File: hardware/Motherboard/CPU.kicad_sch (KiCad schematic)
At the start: 16 parts, among them U1 MC6809, U10 74LS138, U2 27C64, U3 74LS245, U4 74LS139, U5 74LS20, U6 74LS08, U7 74LS02, U8 74LS00, U9 74LS541

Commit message: wip
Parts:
- removed unit 4 of U7
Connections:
- net SYS_ROM_BK: now reaches U2.2 (A12)
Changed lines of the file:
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@@
 	)
 	(junction
-		(at 226.06 162.56)
+		(at 322.58 82.55)
 		(diameter 0)
 		(color 0 0 0 0)
 	)
 	(junction
-		(at 322.58 82.55)
+		(at 215.9 151.13)
 		(diameter 0)
 		(color 0 0 0 0)
@@
 		(color 0 0 0 0)
 	)
-	(junction
-		(at 210.82 151.13)
-		(diameter 0)
-		(color 0 0 0 0)
-	)
 	(no_connect
 		(at 177.8 247.65)
@@
 	(wire
 		(pts
-			(xy 210.82 162.56) (xy 226.06 162.56)
-		)
-		(stroke
-			(width 0)
-			(type default)
-		)
-	)
-	(wire
-		(pts
 			(xy 177.8 232.41) (xy 189.23 232.41)
 		)
@@
 		)
 	)
+	(wire
+		(pts
+			(xy 176.53 30.48) (xy 176.53 91.44)
+		)
+		(stroke
+			(width 0)
+			(type default)
+		)
+	)
 	(polyline
 		(pts
@@
 	(wire
 		(pts
-			(xy 210.82 151.13) (xy 228.6 151.13)
-		)
-		(stroke
-			(width 0)
-			(type default)
-		)
-	)
-	(wire
-		(pts
 			(xy 245.11 130.81) (xy 246.38 130.81)
 		)
@@
 		)
 	)
+	(wire
+		(pts
+			(xy 215.9 151.13) (xy 228.6 151.13)
+		)
+		(stroke
+			(width 0)
+			(type default)
+		)
+	)
 	(polyline
 		(pts
@@
 		)
 	)
+	(wire
+		(pts
+			(xy 176.53 91.44) (xy 186.69 91.44)
+		)
+		(stroke
+			(width 0)
+			(type default)
+		)
+	)
 	(polyline
 		(pts
@@
 	(wire
 		(pts
-			(xy 210.82 151.13) (xy 210.82 162.56)
+			(xy 215.9 151.13) (xy 215.9 162.56)
 		)
 		(stroke
@@
 	(wire
 		(pts
-			(xy 210.82 151.13) (xy 209.55 151.13)
+			(xy 209.55 151.13) (xy 215.9 151.13)
 		)
 		(stroke
@@
 	(wire
 		(pts
+			(xy 215.9 162.56) (xy 269.24 162.56)
+		)
+		(stroke
+			(width 0)
+			(type default)
+		)
+	)
+	(wire
+		(pts
 			(xy 185.42 115.57) (xy 246.38 115.57)
 		)
@@
 		)
 	)
-	(wire
-		(pts
-			(xy 226.06 160.02) (xy 228.6 160.02)
-		)
-		(stroke
-			(width 0)
-			(type default)
-		)
-	)
 	(polyline
 		(pts
@@
 		)
 	)
-	(wire
-		(pts
-			(xy 243.84 162.56) (xy 269.24 162.56)
-		)
-		(stroke
-			(width 0)
-			(type default)
-		)
-	)
 	(bus
 		(pts
@@
 		)
 	)
-	(wire
-		(pts
-			(xy 226.06 162.56) (xy 226.06 160.02)
-		)
-		(stroke
-			(width 0)
-			(type default)
-		)
-	)
 	(bus
 		(pts
@@
 	(wire
 		(pts
-			(xy 228.6 165.1) (xy 226.06 165.1)
-		)
-		(stroke
-			(width 0)
-			(type default)
-		)
-	)
-	(wire
-		(pts
 			(xy 69.85 78.74) (xy 69.85 85.09)
 		)
@@
 		)
 	)
+	(wire
+		(pts
+			(xy 30.48 30.48) (xy 176.53 30.48)
+		)
+		(stroke
+			(width 0)
+			(type default)
+		)
+	)
 	(bus
 		(pts
@@
 	(wire
 		(pts
-			(xy 226.06 165.1) (xy 226.06 162.56)
-		)
-		(stroke
-			(width 0)
-			(type default)
-		)
-	)
-	(wire
-		(pts
 			(xy 325.12 102.87) (xy 335.28 102.87)
 		)
@@
 		)
 	)
-	(label "VMA"
-		(at 264.16 162.56 0)
-		(effects
-			(font
-				(size 1.27 1.27)
-			)
-			(justify left bottom)
-		)
-	)
 	(label "A[15..0]"
 		(at 153.67 44.45 0)
@@
 		)
 	)
-	(hierarchical_label "VMA"
+	(hierarchical_label "~{VMA}"
 		(shape output)
 		(at 269.24 162.56 0)
@@
 		)
 	)
+	(hierarchical_label "SYS_ROM_BK"
+		(shape input)
+		(at 30.48 30.48 180)
+		(effects
+			(font
+				(size 1.27 1.27)
+			)
+			(justify right)
+		)
+	)
 	(hierarchical_label "R~{W}B"
 		(shape output)
@@
 				)
 			)
-		)
-	)
-	(symbol
-		(lib_id "74xx:74LS02")
-		(at 236.22 162.56 0)
-		(unit 4)
-		(exclude_from_sim no)
-		(in_bom yes)
-		(on_board yes)
-		(dnp no)
-		(fields_autoplaced yes)
-		(property "Reference" "U7"
-			(at 236.22 153.67 0)
-			(effects
-				(font
-					(size 1.27 1.27)
-				)
-			)
-		)
-		(property "Value" "74LS02"
-			(at 236.22 156.21 0)
-			(effects
-				(font
-					(size 1.27 1.27)
-				)
-			)
-		)
-		(property "Footprint" ""
-			(at 236.22 162.56 0)
-			(effects
-				(font
-					(size 1.27 1.27)
-				)
-				(hide yes)
-			)
-		)
-		(property "Datasheet" "http://www.ti.com/lit/gpn/sn74ls02"
-			(at 236.22 162.56 0)
-			(effects
-				(font
-					(size 1.27 1.27)
-				)
-				(hide yes)
-			)
-		)
-		(property "Description" "quad 2-input NOR gate"
-			(at 236.22 162.56 0)
-			(effects
-				(font
-					(size 1.27 1.27)
-				)
-				(hide yes)
-			)
-		)
-		(pin "9"
-		)
-		(pin "4"
-		)
-		(pin "12"
-		)
-		(pin "13"
-		)
-		(pin "6"
-		)
-		(pin "10"
-		)
-		(pin "5"
-		)
-		(pin "1"
-		)
-		(pin "3"
-		)
-		(pin "2"
-		)
-		(pin "8"
-		)
-		(pin "7"
-		)
-		(pin "11"
-		)
-		(pin "14"
-		)
-		(instances
-			(project "Squale"
-				(path "/9e981419-a202-4dd8-b7ec-e1bde8e7b185/4df00b19-92a0-4514-ae0b-8cd7ab14a127"
-					(reference "U7")
-					(unit 4)
-				)
-			)

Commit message: WIP : passives parts, cosmetic stuffs.
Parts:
- added C32, C33, C35: 100nF, symbol Device:C
- added unit 3 of U4
- added U66: 74LS273, symbol 74xx:74LS273
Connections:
- net PD0: now also U66.3 (D0)
- net PD1: now also U66.4 (D1)
- net PD2: now also U66.7 (D2)
- net PD3: now also U66.8 (D3)
- net PD4: now also U66.13 (D4)
- net PD5: now also U66.14 (D5)
- net PD6: now also U66.17 (D6)
- net PD7: now also U66.18 (D7)
- net SYS_ROM_BK: now also U66.19 (Q7)
- net VCC5V: now also C32.1, C33.1, C35.1, U4.16 (VCC), U66.20 (VCC)
- net VSS: now also C32.2, C33.2, C35.2, U4.8 (GND), U66.10 (GND)
- net ~{CS_REG}: now also U66.11 (Cp)
- new net SYS_COL0: U66.2 (Q0)
- new net SYS_COL1: U66.5 (Q1)
- new net SYS_COL2: U66.6 (Q2)
- new net SYS_COL3: U66.9 (Q3)
- new net SYS_KEYB_LED: U66.16 (Q6)
- new net SYS_MDM_LINE: U66.15 (Q5)
- new net SYS_MDM_MC_~{BC}: U66.12 (Q4)
- new net ~{RSTB}: U66.1 (~{Mr})
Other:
- note added: "System control register Base :0xF010"
- moved on the sheet: C16, D3, R42, R43, R44, R45, U1, U10, U2, U3, U4A, U4B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

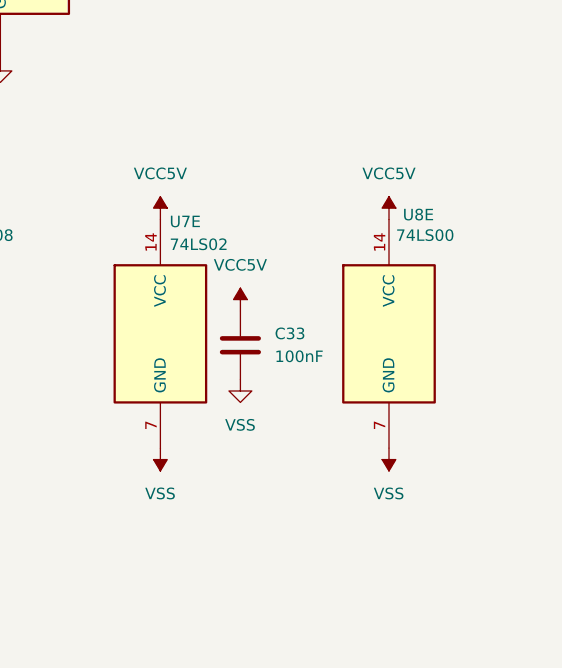
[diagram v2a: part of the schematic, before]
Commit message: duplicated U8E
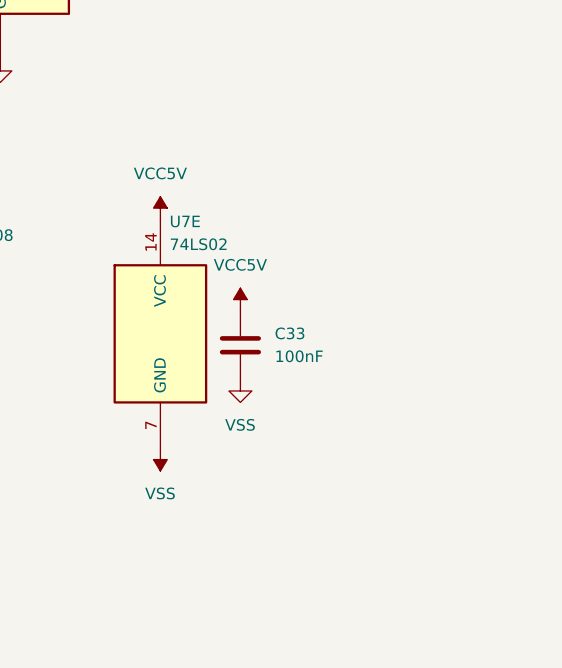
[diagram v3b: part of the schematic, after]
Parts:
- removed unit 5 of U8
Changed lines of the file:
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@@
-	)
-	(symbol
-		(lib_id "power:VSS")
-		(at 393.7 240.03 180)
-		(unit 1)
-		(exclude_from_sim no)
-		(in_bom yes)
-		(on_board yes)
-		(dnp no)
-		(property "Reference" "#PWR0163"
-			(at 393.7 236.22 0)
-			(effects
-				(font
-					(size 1.27 1.27)
-				)
-				(hide yes)
-			)
-		)
-		(property "Value" "VSS"
-			(at 393.7 245.11 0)
-			(effects
-				(font
-					(size 1.27 1.27)
-				)
-			)
-		)
-		(property "Footprint" ""
-			(at 393.7 240.03 0)
-			(effects
-				(font
-					(size 1.27 1.27)
-				)
-				(hide yes)
-			)
-		)
-		(property "Datasheet" ""
-			(at 393.7 240.03 0)
-			(effects
-				(font
-					(size 1.27 1.27)
-				)
-				(hide yes)
-			)
-		)
-		(property "Description" "Power symbol creates a global label with name \"VSS\""
-			(at 393.7 240.03 0)
-			(effects
-				(font
-					(size 1.27 1.27)
-				)
-				(hide yes)
-			)
-		)
-		(pin "1"
-		)
-		(instances
-			(project "Squale"
-				(path "/9e981419-a202-4dd8-b7ec-e1bde8e7b185/4df00b19-92a0-4514-ae0b-8cd7ab14a127"
-					(reference "#PWR0163")
-					(unit 1)
-				)
-			)
-		)
 	)
 	(symbol
@@
 	)
 	(symbol
-		(lib_id "power:VSS")
-		(at 393.7 214.63 0)
-		(unit 1)
-		(exclude_from_sim no)
-		(in_bom yes)
-		(on_board yes)
-		(dnp no)
-		(fields_autoplaced yes)
-		(property "Reference" "#PWR0150"
-			(at 393.7 218.44 0)
-			(effects
-				(font
-					(size 1.27 1.27)
-				)
-				(hide yes)
-			)
-		)
-		(property "Value" "VCC5V"
-			(at 393.7 209.55 0)
-			(effects
-				(font
-					(size 1.27 1.27)
-				)
-			)
-		)
-		(property "Footprint" ""
-			(at 393.7 214.63 0)
-			(effects
-				(font
-					(size 1.27 1.27)
-				)
-				(hide yes)
-			)
-		)
-		(property "Datasheet" ""
-			(at 393.7 214.63 0)
-			(effects
-				(font
-					(size 1.27 1.27)
-				)
-				(hide yes)
-			)
-		)
-		(property "Description" "Power symbol creates a global label with name \"VSS\""
-			(at 393.7 214.63 0)
-			(effects
-				(font
-					(size 1.27 1.27)
-				)
-				(hide yes)
-			)
-		)
-		(pin "1"
-		)
-		(instances
-			(project "Squale"
-				(path "/9e981419-a202-4dd8-b7ec-e1bde8e7b185/4df00b19-92a0-4514-ae0b-8cd7ab14a127"
-					(reference "#PWR0150")
-					(unit 1)
-				)
-			)
-		)
-	)
-	(symbol
 		(lib_id "74xx:74LS20")
 		(at 162.56 129.54 0)
@@
 				)
 			)
-		)
-	)
-	(symbol
-		(lib_id "74xx:74LS00")
-		(at 393.7 227.33 0)
-		(unit 5)
-		(exclude_from_sim no)
-		(in_bom yes)
-		(on_board yes)
-		(dnp no)
-		(property "Reference" "U8"
-			(at 395.224 214.122 0)
-			(effects
-				(font
-					(size 1.27 1.27)
-				)
-				(justify left)
-			)
-		)
-		(property "Value" "74LS00"
-			(at 394.462 216.408 0)
-			(effects
-				(font
-					(size 1.27 1.27)
-				)
-				(justify left)
-			)
-		)
-		(property "Footprint" ""
-			(at 393.7 227.33 0)
-			(effects
-				(font
-					(size 1.27 1.27)
-				)
-				(hide yes)
-			)
-		)
-		(property "Datasheet" "http://www.ti.com/lit/gpn/sn74ls00"
-			(at 393.7 227.33 0)
-			(effects
-				(font
-					(size 1.27 1.27)
-				)
-				(hide yes)
-			)
-		)
-		(property "Description" "quad 2-input NAND gate"
-			(at 393.7 227.33 0)
-			(effects
-				(font
-					(size 1.27 1.27)
-				)
-				(hide yes)
-			)
-		)
-		(pin "14"
-		)
-		(pin "13"
-		)
-		(pin "1"
-		)
-		(pin "10"
-		)
-		(pin "4"
-		)
-		(pin "2"
-		)
-		(pin "3"
-		)
-		(pin "12"
-		)
-		(pin "8"
-		)
-		(pin "7"
-		)
-		(pin "6"
-		)
-		(pin "9"
-		)
-		(pin "11"
-		)
-		(pin "5"
-		)
-		(instances
-			(project "Squale"
-				(path "/9e981419-a202-4dd8-b7ec-e1bde8e7b185/4df00b19-92a0-4514-ae0b-8cd7ab14a127"
-					(reference "U8")
-					(unit 5)
-				)
-			)

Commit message: Footprints.
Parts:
- C16: footprint (none) -> Capacitor_THT:C_Radial_D6.3mm_H5.0mm_P2.50mm
- C32, C33, C35: footprint (none) -> Capacitor_THT:C_Disc_D9.0mm_W2.5mm_P5.00mm
- R42, R43, R44, R45: footprint (none) -> Resistor_THT:R_Axial_DIN0309_L9.0mm_D3.2mm_P12.70mm_Horizontal
- U1: footprint Package_DIP:DIP-40_W15.24mm -> Package_DIP:DIP-40_W15.24mm_Socket
- U10, U4: footprint (none) -> Package_DIP:DIP-16_W7.62mm_Socket
- U2: footprint Package_DIP:DIP-28_W15.24mm -> Package_DIP:DIP-28_W15.24mm_Socket
- U3, U66, U9: footprint (none) -> Package_DIP:DIP-20_W7.62mm_Socket
- U5, U6, U7, U8: footprint (none) -> Package_DIP:DIP-14_W7.62mm_Socket
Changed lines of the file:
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@@
 			)
 		)
-		(property "Footprint" ""
+		(property "Footprint" "Package_DIP:DIP-20_W7.62mm_Socket"
 			(at 350.52 176.53 0)
 			(effects
@@
 			)
 		)
-		(property "Footprint" ""
+		(property "Footprint" "Package_DIP:DIP-14_W7.62mm_Socket"
 			(at 204.47 148.59 0)
 			(effects
@@
 			)
 		)
-		(property "Footprint" ""
+		(property "Footprint" "Package_DIP:DIP-16_W7.62mm_Socket"
 			(at 167.64 175.26 0)
 			(effects
@@
 			)
 		)
-		(property "Footprint" ""
+		(property "Footprint" "Package_DIP:DIP-14_W7.62mm_Socket"
 			(at 256.54 146.05 0)
 			(effects
@@
 			)
 		)
-		(property "Footprint" ""
+		(property "Footprint" "Capacitor_THT:C_Disc_D9.0mm_W2.5mm_P5.00mm"
 			(at 224.4852 58.42 0)
 			(effects
@@
 			)
 		)
-		(property "Footprint" ""
+		(property "Footprint" "Package_DIP:DIP-14_W7.62mm_Socket"
 			(at 186.69 205.74 0)
 			(effects
@@
 			)
 		)
-		(property "Footprint" ""
+		(property "Footprint" "Package_DIP:DIP-14_W7.62mm_Socket"
 			(at 320.04 227.33 0)
 			(effects
@@
 			)
 		)
-		(property "Footprint" ""
+		(property "Footprint" "Package_DIP:DIP-14_W7.62mm_Socket"
 			(at 344.17 227.33 0)
 			(effects
@@
 			)
 		)
-		(property "Footprint" ""
+		(property "Footprint" "Package_DIP:DIP-20_W7.62mm_Socket"
 			(at 350.52 50.8 0)
 			(effects
@@
 			)
 		)
-		(property "Footprint" ""
+		(property "Footprint" "Package_DIP:DIP-14_W7.62mm_Socket"
 			(at 238.76 146.05 0)
 			(effects
@@
 			)
 		)
-		(property "Footprint" ""
+		(property "Footprint" "Package_DIP:DIP-16_W7.62mm_Socket"
 			(at 295.91 227.33 0)
 			(effects
@@
 			)
 		)
-		(property "Footprint" ""
+		(property "Footprint" "Package_DIP:DIP-14_W7.62mm_Socket"
 			(at 162.56 129.54 0)
 			(effects
@@
 			)
 		)
-		(property "Footprint" ""
+		(property "Footprint" "Package_DIP:DIP-14_W7.62mm_Socket"
 			(at 256.54 115.57 0)
 			(effects
@@
 			)
 		)
-		(property "Footprint" "Package_DIP:DIP-28_W15.24mm"
+		(property "Footprint" "Package_DIP:DIP-28_W15.24mm_Socket"
 			(at 199.39 78.74 0)
 			(effects
@@
 			)
 		)
-		(property "Footprint" ""
+		(property "Footprint" "Package_DIP:DIP-16_W7.62mm_Socket"
 			(at 167.64 153.67 0)
 			(effects
@@
 			)
 		)
-		(property "Footprint" ""
+		(property "Footprint" "Resistor_THT:R_Axial_DIN0309_L9.0mm_D3.2mm_P12.70mm_Horizontal"
 			(at 94.488 72.39 90)
 			(effects
@@
 			)
 		)
-		(property "Footprint" ""
+		(property "Footprint" "Resistor_THT:R_Axial_DIN0309_L9.0mm_D3.2mm_P12.70mm_Horizontal"
 			(at 74.168 72.39 90)
 			(effects
@@
 			)
 		)
-		(property "Footprint" ""
+		(property "Footprint" "Resistor_THT:R_Axial_DIN0309_L9.0mm_D3.2mm_P12.70mm_Horizontal"
 			(at 55.372 60.96 90)
 			(effects
@@
 			)
 		)
-		(property "Footprint" ""
+		(property "Footprint" "Package_DIP:DIP-14_W7.62mm_Socket"
 			(at 368.3 227.33 0)
 			(effects
@@
 			)
 		)
-		(property "Footprint" ""
+		(property "Footprint" "Package_DIP:DIP-14_W7.62mm_Socket"
 			(at 285.75 173.99 0)
 			(effects
@@
 			)
 		)
-		(property "Footprint" ""
+		(property "Footprint" "Package_DIP:DIP-14_W7.62mm_Socket"
 			(at 220.98 173.99 0)
 			(effects
@@
 			)
 		)
-		(property "Footprint" ""
+		(property "Footprint" "Package_DIP:DIP-14_W7.62mm_Socket"
 			(at 284.48 260.35 0)
 			(effects
@@
 			)
 		)
-		(property "Footprint" ""
+		(property "Footprint" "Package_DIP:DIP-16_W7.62mm_Socket"
 			(at 167.64 234.95 0)
 			(effects
@@
 			)
 		)
-		(property "Footprint" ""
+		(property "Footprint" "Capacitor_THT:C_Disc_D9.0mm_W2.5mm_P5.00mm"
 			(at 378.1552 232.41 0)
 			(effects
@@
 			)
 		)
-		(property "Footprint" ""
+		(property "Footprint" "Package_DIP:DIP-14_W7.62mm_Socket"
 			(at 256.54 130.81 0)
 			(effects
@@
 			)
 		)
-		(property "Footprint" ""
+		(property "Footprint" "Package_DIP:DIP-14_W7.62mm_Socket"
 			(at 165.1 208.28 0)
 			(effects
@@
 			)
 		)
-		(property "Footprint" ""
+		(property "Footprint" "Capacitor_THT:C_Disc_D9.0mm_W2.5mm_P5.00mm"
 			(at 91.1352 48.26 0)
 			(effects
@@
 			)
 		)
-		(property "Footprint" ""
+		(property "Footprint" "Resistor_THT:R_Axial_DIN0309_L9.0mm_D3.2mm_P12.70mm_Horizontal"
 			(at 84.328 72.39 90)
 			(effects
@@
 			)
 		)
-		(property "Footprint" "Package_DIP:DIP-40_W15.24mm"
+		(property "Footprint" "Package_DIP:DIP-40_W15.24mm_Socket"
 			(at 121.92 125.73 0)
 			(effects
@@
 			)
 		)
-		(property "Footprint" ""
+		(property "Footprint" "Package_DIP:DIP-20_W7.62mm_Socket"
 			(at 350.52 114.3 0)
 			(effects
@@
 			)
 		)
-		(property "Footprint" ""
+		(property "Footprint" "Capacitor_THT:C_Radial_D6.3mm_H5.0mm_P2.50mm"
 			(at 46.6852 76.2 0)
 			(effects
